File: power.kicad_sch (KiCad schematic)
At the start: 9 parts

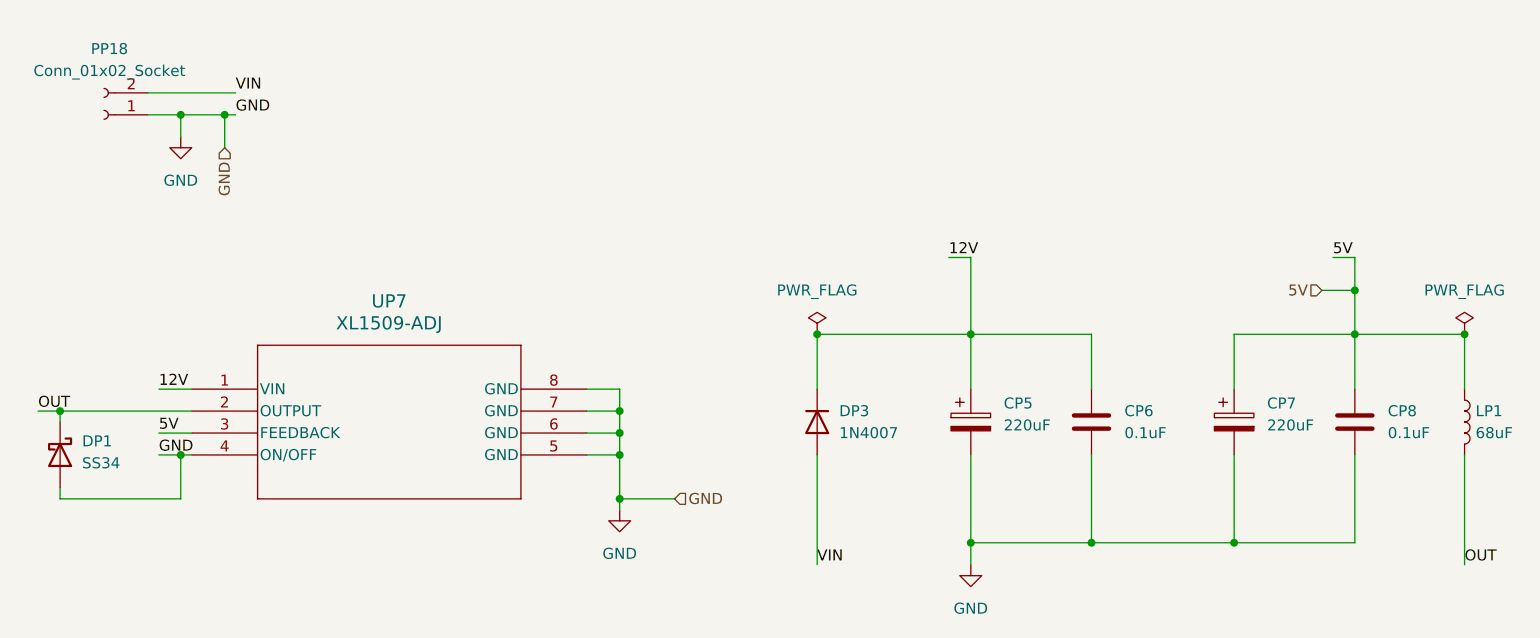
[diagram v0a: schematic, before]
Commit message: feat: integrated rtc ldc i2c / fixed 12v power line rs485 / output com pin -> input power type
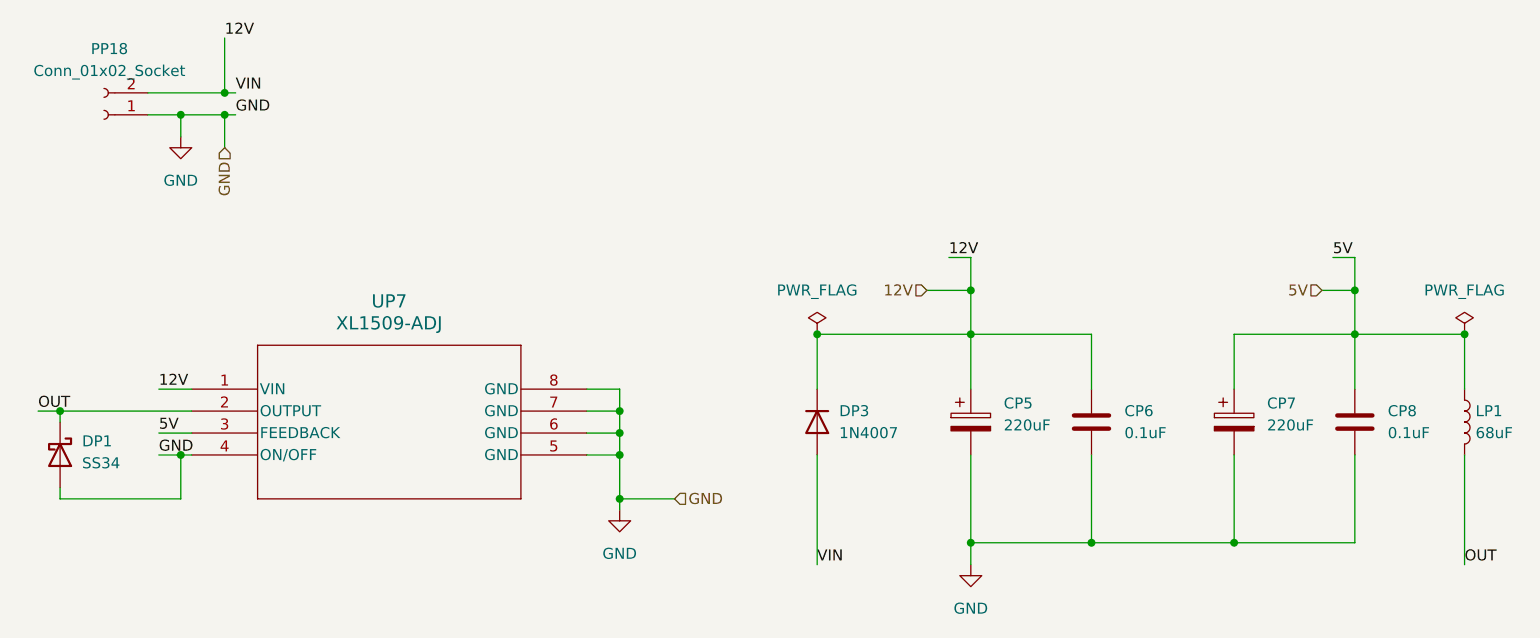
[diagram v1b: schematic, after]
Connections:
- net VIN is gone; now on net 12V: DP3.2 (A), PP18.2 (Pin_2)
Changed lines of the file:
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@@
+	)
+	(junction
+		(at 88.9 64.77)
+		(diameter 0)
+		(color 0 0 0 0)
 	)
 	(junction
@@
 	)
 	(junction
+		(at 175.26 87.63)
+		(diameter 0)
+		(color 0 0 0 0)
+	)
+	(junction
 		(at 219.71 92.71)
 		(diameter 0)
@@
 	(wire
 		(pts
-			(xy 175.26 83.82) (xy 175.26 92.71)
+			(xy 175.26 83.82) (xy 175.26 87.63)
 		)
 		(stroke
@@
 	(wire
 		(pts
-			(xy 80.01 64.77) (xy 90.17 64.77)
+			(xy 80.01 64.77) (xy 88.9 64.77)
 		)
 		(stroke
@@
 	(wire
 		(pts
+			(xy 88.9 64.77) (xy 90.17 64.77)
+		)
+		(stroke
+			(width 0)
+			(type default)
+		)
+	)
+	(wire
+		(pts
 			(xy 217.17 83.82) (xy 219.71 83.82)
 		)
@@
 	(wire
 		(pts
+			(xy 175.26 87.63) (xy 175.26 92.71)
+		)
+		(stroke
+			(width 0)
+			(type default)
+		)
+	)
+	(wire
+		(pts
+			(xy 88.9 58.42) (xy 88.9 64.77)
+		)
+		(stroke
+			(width 0)
+			(type default)
+		)
+	)
+	(wire
+		(pts
 			(xy 219.71 92.71) (xy 219.71 99.06)
 		)
@@
 		(pts
 			(xy 175.26 92.71) (xy 189.23 92.71)
+		)
+		(stroke
+			(width 0)
+			(type default)
+		)
+	)
+	(wire
+		(pts
+			(xy 170.18 87.63) (xy 175.26 87.63)
 		)
 		(stroke
@@
 	(label "VIN"
 		(at 157.48 119.38 0)
+		(effects
+			(font
+				(size 1.27 1.27)
+			)
+			(justify left bottom)
+		)
+	)
+	(label "12V"
+		(at 88.9 58.42 0)
 		(effects
 			(font
@@
 		)
 	)
+	(hierarchical_label "12V"
+		(shape input)
+		(at 170.18 87.63 180)
+		(effects
+			(font
+				(size 1.27 1.27)
+			)
+			(justify right)
+		)
+	)

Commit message: draft:updating pcb dimentions
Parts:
- renumbered DP1 to SDP1
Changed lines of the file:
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@@
 		(dnp no)
 		(fields_autoplaced yes)
-		(property "Reference" "DP1"
+		(property "Reference" "SDP1"
 			(at 72.39 105.0924 90)
 			(effects
@@
 			(project ""
 				(path "/a1c80da3-9403-4ec6-a34a-1db23a22b009/2927ccdf-c553-42db-bc8e-c4c5c9181f4b"
-					(reference "DP1")
+					(reference "SDP1")
 					(unit 1)
 				)
